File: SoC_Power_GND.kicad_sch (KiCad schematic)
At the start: 4 parts, among them U1 rv1126/rv1109

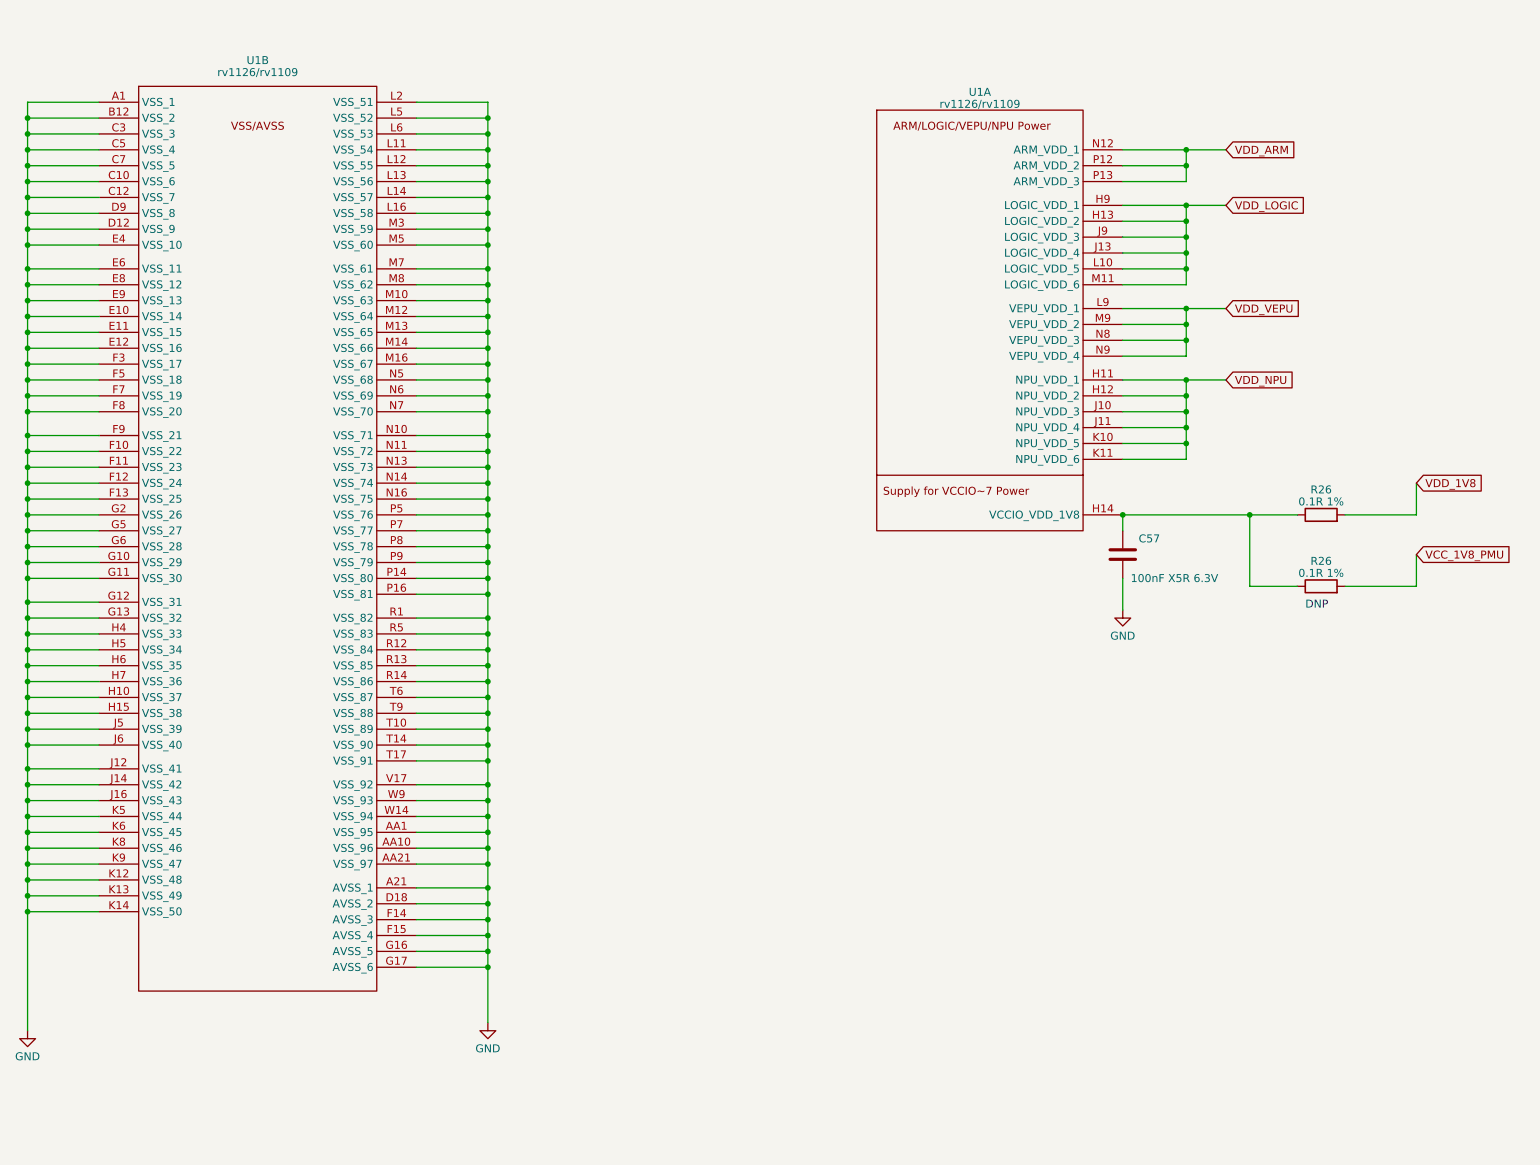
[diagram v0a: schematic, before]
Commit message: updated Power GND
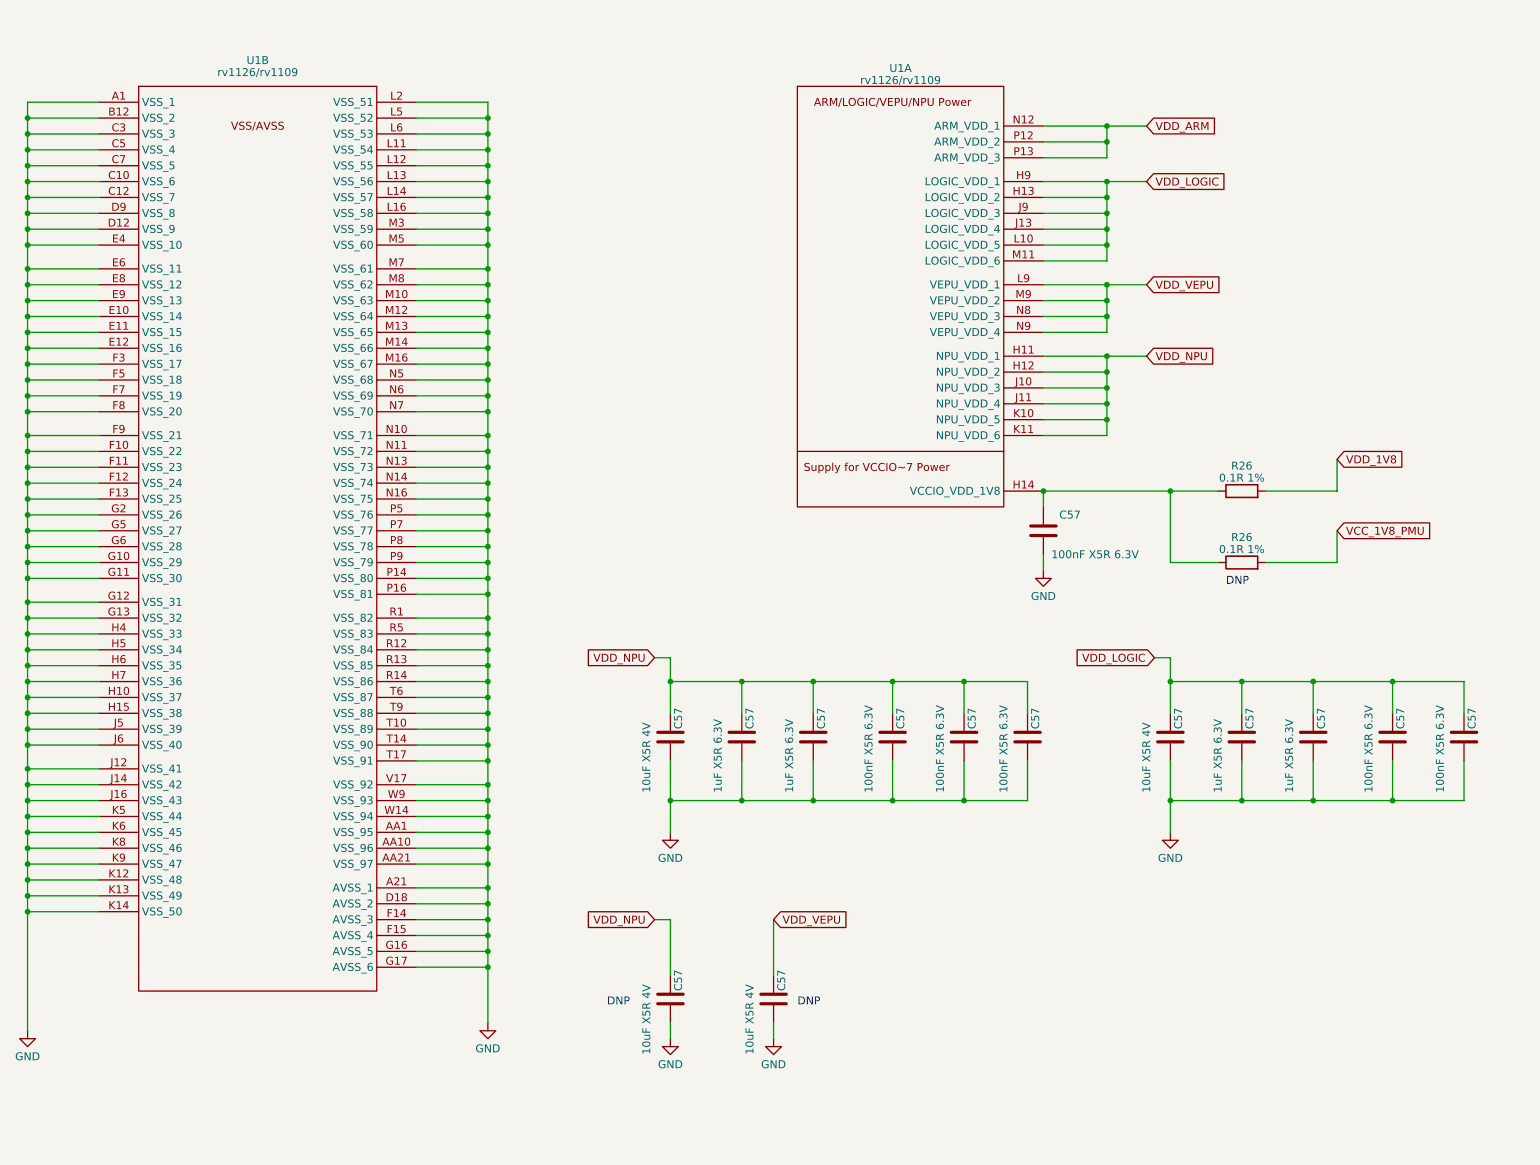
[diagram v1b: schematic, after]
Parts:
- added C57 (x4): 10uF X5R 4V, Capacitor_SMD:C_0402_1005Metric, symbol Device:C
- added C57 (x5): 100nF X5R 6.3V, Capacitor_SMD:C_0201_0603Metric, symbol Device:C
- added C57 (x4): 1uF X5R 6.3V, Capacitor_SMD:C_0402_1005Metric, symbol Device:C
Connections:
- net GND: now also C57.2, C57.2, C57.2, C57.2, C57.2, C57.2, C57.2, C57.2, C57.2, C57.2, C57.2, C57.2, C57.2
- net VDD_LOGIC: now also C57.1, C57.1, C57.1, C57.1, C57.1
- net VDD_NPU: now also C57.1, C57.1, C57.1, C57.1, C57.1, C57.1, C57.1
- net VDD_VEPU: now also C57.1
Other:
- moved on the sheet: C57, R26, U1A

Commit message: added MicroSD
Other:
- note added: "NOTE: If any power domain of VCCIO 1~7 is used, then VCCIO_VDD_1V8 must be connected to 1.8V power supply"
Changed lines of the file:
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@@
     (effects (font (size 1.27 1.27) (color 221 133 0 1)) (justify left bottom))
+  )
+  (text "NOTE:\nIf any power domain of VCCIO 1~7 is used, \nthen VCCIO_VDD_1V8 must be connected to \n1.8V power supply"
+    (at 148.59 104.14 0)
+    (effects (font (size 1.27 1.27) (color 194 194 0 1)) (justify left bottom))
   )
   (text "DNP" (at 234.95 105.41 0)

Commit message: updated footprints
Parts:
- U1: footprint (none) -> Rockchip_SoC:Rockchip_RV1126_FCCSP409LD_14.0x14.0mm
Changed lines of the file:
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@@
         )
         (path "/e3b58043-16a3-43c8-9fad-9c9784eebfa4/cc9fb3ac-19c3-47a8-ba7d-678b4d514ff0/8aa2eca1-edfe-4e9d-a854-96f51e82fbdb"
-          (reference "C95") (unit 1)
+          (reference "C38") (unit 1)
         )
       )
@@
         )
         (path "/e3b58043-16a3-43c8-9fad-9c9784eebfa4/cc9fb3ac-19c3-47a8-ba7d-678b4d514ff0/8aa2eca1-edfe-4e9d-a854-96f51e82fbdb"
-          (reference "C99") (unit 1)
+          (reference "C42") (unit 1)
         )
       )
@@
         )
         (path "/e3b58043-16a3-43c8-9fad-9c9784eebfa4/cc9fb3ac-19c3-47a8-ba7d-678b4d514ff0/8aa2eca1-edfe-4e9d-a854-96f51e82fbdb"
-          (reference "#PWR072") (unit 1)
+          (reference "#PWR060") (unit 1)
         )
       )
@@
       (effects (font (size 1.27 1.27)))
     )
-    (property "Footprint" "" (at 200.66 91.44 0)
+    (property "Footprint" "Rockchip_SoC:Rockchip_RV1126_FCCSP409LD_14.0x14.0mm" (at 200.66 91.44 0)
       (effects (font (size 1.27 1.27)) hide)
     )
@@
         )
         (path "/e3b58043-16a3-43c8-9fad-9c9784eebfa4/cc9fb3ac-19c3-47a8-ba7d-678b4d514ff0/8aa2eca1-edfe-4e9d-a854-96f51e82fbdb"
-          (reference "R33") (unit 1)
+          (reference "R36") (unit 1)
         )
       )
@@
         )
         (path "/e3b58043-16a3-43c8-9fad-9c9784eebfa4/cc9fb3ac-19c3-47a8-ba7d-678b4d514ff0/8aa2eca1-edfe-4e9d-a854-96f51e82fbdb"
-          (reference "C90") (unit 1)
+          (reference "C34") (unit 1)
         )
       )
@@
         )
         (path "/e3b58043-16a3-43c8-9fad-9c9784eebfa4/cc9fb3ac-19c3-47a8-ba7d-678b4d514ff0/8aa2eca1-edfe-4e9d-a854-96f51e82fbdb"
-          (reference "C1") (unit 1)
+          (reference "C29") (unit 1)
         )
       )
@@
         )
         (path "/e3b58043-16a3-43c8-9fad-9c9784eebfa4/cc9fb3ac-19c3-47a8-ba7d-678b4d514ff0/8aa2eca1-edfe-4e9d-a854-96f51e82fbdb"
-          (reference "#PWR071") (unit 1)
+          (reference "#PWR058") (unit 1)
         )
       )
@@
         )
         (path "/e3b58043-16a3-43c8-9fad-9c9784eebfa4/cc9fb3ac-19c3-47a8-ba7d-678b4d514ff0/8aa2eca1-edfe-4e9d-a854-96f51e82fbdb"
-          (reference "#PWR03") (unit 1)
+          (reference "#PWR056") (unit 1)
         )
       )
@@
         )
         (path "/e3b58043-16a3-43c8-9fad-9c9784eebfa4/cc9fb3ac-19c3-47a8-ba7d-678b4d514ff0/8aa2eca1-edfe-4e9d-a854-96f51e82fbdb"
-          (reference "C98") (unit 1)
+          (reference "C41") (unit 1)
         )
       )
@@
         )
         (path "/e3b58043-16a3-43c8-9fad-9c9784eebfa4/cc9fb3ac-19c3-47a8-ba7d-678b4d514ff0/8aa2eca1-edfe-4e9d-a854-96f51e82fbdb"
-          (reference "C94") (unit 1)
+          (reference "C32") (unit 1)
         )
       )
@@
         )
         (path "/e3b58043-16a3-43c8-9fad-9c9784eebfa4/cc9fb3ac-19c3-47a8-ba7d-678b4d514ff0/8aa2eca1-edfe-4e9d-a854-96f51e82fbdb"
-          (reference "C87") (unit 1)
+          (reference "C37") (unit 1)
         )
       )
@@
         )
         (path "/e3b58043-16a3-43c8-9fad-9c9784eebfa4/cc9fb3ac-19c3-47a8-ba7d-678b4d514ff0/8aa2eca1-edfe-4e9d-a854-96f51e82fbdb"
-          (reference "#PWR01") (unit 1)
+          (reference "#PWR054") (unit 1)
         )
       )
@@
         )
         (path "/e3b58043-16a3-43c8-9fad-9c9784eebfa4/cc9fb3ac-19c3-47a8-ba7d-678b4d514ff0/8aa2eca1-edfe-4e9d-a854-96f51e82fbdb"
-          (reference "#PWR069") (unit 1)
+          (reference "#PWR059") (unit 1)
         )
       )
@@
       (effects (font (size 1.27 1.27)))
     )
-    (property "Footprint" "" (at 97.79 90.17 0)
+    (property "Footprint" "Rockchip_SoC:Rockchip_RV1126_FCCSP409LD_14.0x14.0mm" (at 97.79 90.17 0)
       (effects (font (size 1.27 1.27)) hide)
     )
@@
         )
         (path "/e3b58043-16a3-43c8-9fad-9c9784eebfa4/cc9fb3ac-19c3-47a8-ba7d-678b4d514ff0/8aa2eca1-edfe-4e9d-a854-96f51e82fbdb"
-          (reference "#PWR070") (unit 1)
+          (reference "#PWR057") (unit 1)
         )
       )
@@
         )
         (path "/e3b58043-16a3-43c8-9fad-9c9784eebfa4/cc9fb3ac-19c3-47a8-ba7d-678b4d514ff0/8aa2eca1-edfe-4e9d-a854-96f51e82fbdb"
-          (reference "#PWR02") (unit 1)
+          (reference "#PWR055") (unit 1)
         )
       )
@@
         )
         (path "/e3b58043-16a3-43c8-9fad-9c9784eebfa4/cc9fb3ac-19c3-47a8-ba7d-678b4d514ff0/8aa2eca1-edfe-4e9d-a854-96f51e82fbdb"
-          (reference "C93") (unit 1)
+          (reference "C30") (unit 1)
         )
       )
@@
         )
         (path "/e3b58043-16a3-43c8-9fad-9c9784eebfa4/cc9fb3ac-19c3-47a8-ba7d-678b4d514ff0/8aa2eca1-edfe-4e9d-a854-96f51e82fbdb"
-          (reference "C91") (unit 1)
+          (reference "C35") (unit 1)
         )
       )
@@
         )
         (path "/e3b58043-16a3-43c8-9fad-9c9784eebfa4/cc9fb3ac-19c3-47a8-ba7d-678b4d514ff0/8aa2eca1-edfe-4e9d-a854-96f51e82fbdb"
-          (reference "C97") (unit 1)
+          (reference "C40") (unit 1)
         )
       )
@@
         )
         (path "/e3b58043-16a3-43c8-9fad-9c9784eebfa4/cc9fb3ac-19c3-47a8-ba7d-678b4d514ff0/8aa2eca1-edfe-4e9d-a854-96f51e82fbdb"
-          (reference "C88") (unit 1)
+          (reference "C31") (unit 1)
         )
       )
@@
         )
         (path "/e3b58043-16a3-43c8-9fad-9c9784eebfa4/cc9fb3ac-19c3-47a8-ba7d-678b4d514ff0/8aa2eca1-edfe-4e9d-a854-96f51e82fbdb"
-          (reference "C89") (unit 1)
+          (reference "C33") (unit 1)
         )
       )
@@
         )
         (path "/e3b58043-16a3-43c8-9fad-9c9784eebfa4/cc9fb3ac-19c3-47a8-ba7d-678b4d514ff0/8aa2eca1-edfe-4e9d-a854-96f51e82fbdb"
-          (reference "C92") (unit 1)
+          (reference "C36") (unit 1)
         )
       )
@@
         )
         (path "/e3b58043-16a3-43c8-9fad-9c9784eebfa4/cc9fb3ac-19c3-47a8-ba7d-678b4d514ff0/8aa2eca1-edfe-4e9d-a854-96f51e82fbdb"
-          (reference "R34") (unit 1)
+          (reference "R37") (unit 1)
         )
       )
@@
         )
         (path "/e3b58043-16a3-43c8-9fad-9c9784eebfa4/cc9fb3ac-19c3-47a8-ba7d-678b4d514ff0/8aa2eca1-edfe-4e9d-a854-96f51e82fbdb"
-          (reference "C96") (unit 1)
-        )
-      )
+          (reference "C39") (unit 1)
+        )
+      )

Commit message: updated Capacitors
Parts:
- C57: LCSC (none) -> C76934; Model (none) -> GRM033R61A104KE15D; Vendor (none) -> muRata(村田)
- C57: footprint Capacitor_SMD:C_0402_1005Metric -> Capacitor_SMD:C_0201_0603Metric; LCSC (none) -> C76934; Model (none) -> GRM033R61A104KE15D; Vendor (none) -> muRata(村田)
- C57: footprint Capacitor_SMD:C_0402_1005Metric -> Capacitor_SMD:C_0201_0603Metric; LCSC (none) -> C76929; Model (none) -> GRM033R60J105KEA2D; Vendor (none) -> muRata(村田)
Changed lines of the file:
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@@
+      (effects (font (size 1.27 1.27)) hide)
+    )
+    (property "Description" "容值: 100nF 精度: ±10% 额定电压: 10V 材质(温度系数): X5R 材质:X5R" (at 273.05 129.54 0)
+      (effects (font (size 1.27 1.27)) hide)
+    )
+    (property "LCSC" "C76934" (at 273.05 129.54 0)
+      (effects (font (size 1.27 1.27)) hide)
+    )
+    (property "Model" "GRM033R61A104KE15D" (at 273.05 129.54 0)
+      (effects (font (size 1.27 1.27)) hide)
+    )
+    (property "Vendor" "muRata(村田)" (at 273.05 129.54 0)
       (effects (font (size 1.27 1.27)) hide)
     )
@@
       (effects (font (size 1.27 1.27)) hide)
     )
+    (property "Description" "容值: 100nF 精度: ±10% 额定电压: 10V 材质(温度系数): X5R 材质:X5R" (at 181.61 129.54 0)
+      (effects (font (size 1.27 1.27)) hide)
+    )
+    (property "LCSC" "C76934" (at 181.61 129.54 0)
+      (effects (font (size 1.27 1.27)) hide)
+    )
+    (property "Model" "GRM033R61A104KE15D" (at 181.61 129.54 0)
+      (effects (font (size 1.27 1.27)) hide)
+    )
+    (property "Vendor" "muRata(村田)" (at 181.61 129.54 0)
+      (effects (font (size 1.27 1.27)) hide)
+    )
     (pin "1")
     (pin "2")
@@
       (effects (font (size 1.27 1.27)) hide)
     )
+    (property "Description" "容值: 100nF 精度: ±10% 额定电压: 10V 材质(温度系数): X5R 材质:X5R" (at 261.62 129.54 0)
+      (effects (font (size 1.27 1.27)) hide)
+    )
+    (property "LCSC" "C76934" (at 261.62 129.54 0)
+      (effects (font (size 1.27 1.27)) hide)
+    )
+    (property "Model" "GRM033R61A104KE15D" (at 261.62 129.54 0)
+      (effects (font (size 1.27 1.27)) hide)
+    )
+    (property "Vendor" "muRata(村田)" (at 261.62 129.54 0)
+      (effects (font (size 1.27 1.27)) hide)
+    )
     (pin "1")
     (pin "2")
@@
       (effects (font (size 1.27 1.27)) (justify left))
     )
-    (property "Footprint" "Capacitor_SMD:C_0402_1005Metric" (at 206.7052 100.33 0)
+    (property "Footprint" "Capacitor_SMD:C_0201_0603Metric" (at 206.7052 100.33 0)
       (effects (font (size 1.27 1.27)) hide)
     )
     (property "Datasheet" "~" (at 205.74 96.52 0)
+      (effects (font (size 1.27 1.27)) hide)
+    )
+    (property "Description" "容值: 100nF 精度: ±10% 额定电压: 10V 材质(温度系数): X5R 材质:X5R" (at 205.74 96.52 0)
+      (effects (font (size 1.27 1.27)) hide)
+    )
+    (property "LCSC" "C76934" (at 205.74 96.52 0)
+      (effects (font (size 1.27 1.27)) hide)
+    )
+    (property "Model" "GRM033R61A104KE15D" (at 205.74 96.52 0)
+      (effects (font (size 1.27 1.27)) hide)
+    )
+    (property "Vendor" "muRata(村田)" (at 205.74 96.52 0)
       (effects (font (size 1.27 1.27)) hide)
     )
@@
       (effects (font (size 1.27 1.27)) hide)
     )
+    (property "Description" "容值: 100nF 精度: ±10% 额定电压: 10V 材质(温度系数): X5R 材质:X5R" (at 193.04 129.54 0)
+      (effects (font (size 1.27 1.27)) hide)
+    )
+    (property "LCSC" "C76934" (at 193.04 129.54 0)
+      (effects (font (size 1.27 1.27)) hide)
+    )
+    (property "Model" "GRM033R61A104KE15D" (at 193.04 129.54 0)
+      (effects (font (size 1.27 1.27)) hide)
+    )
+    (property "Vendor" "muRata(村田)" (at 193.04 129.54 0)
+      (effects (font (size 1.27 1.27)) hide)
+    )
     (pin "1")
     (pin "2")
@@
       (effects (font (size 1.27 1.27)) (justify left))
     )
-    (property "Footprint" "Capacitor_SMD:C_0402_1005Metric" (at 249.8852 133.35 0)
+    (property "Footprint" "Capacitor_SMD:C_0201_0603Metric" (at 249.8852 133.35 0)
       (effects (font (size 1.27 1.27)) hide)
     )
     (property "Datasheet" "~" (at 248.92 129.54 0)
+      (effects (font (size 1.27 1.27)) hide)
+    )
+    (property "Description" "容值: 1uF 精度: ±10% 额定电压: 6.3V 材质(温度系数): X5R 材质:X5R" (at 248.92 129.54 0)
+      (effects (font (size 1.27 1.27)) hide)
+    )
+    (property "LCSC" "C76929" (at 248.92 129.54 0)
+      (effects (font (size 1.27 1.27)) hide)
+    )
+    (property "Model" "GRM033R60J105KEA2D" (at 248.92 129.54 0)
+      (effects (font (size 1.27 1.27)) hide)
+    )
+    (property "Vendor" "muRata(村田)" (at 248.92 129.54 0)
       (effects (font (size 1.27 1.27)) hide)
     )
@@
       (effects (font (size 1.27 1.27)) (justify left))
     )
-    (property "Footprint" "Capacitor_SMD:C_0402_1005Metric" (at 158.4452 133.35 0)
+    (property "Footprint" "Capacitor_SMD:C_0201_0603Metric" (at 158.4452 133.35 0)
       (effects (font (size 1.27 1.27)) hide)
     )
     (property "Datasheet" "~" (at 157.48 129.54 0)
+      (effects (font (size 1.27 1.27)) hide)
+    )
+    (property "Description" "容值: 1uF 精度: ±10% 额定电压: 6.3V 材质(温度系数): X5R 材质:X5R" (at 157.48 129.54 0)
+      (effects (font (size 1.27 1.27)) hide)
+    )
+    (property "LCSC" "C76929" (at 157.48 129.54 0)
+      (effects (font (size 1.27 1.27)) hide)
+    )
+    (property "Model" "GRM033R60J105KEA2D" (at 157.48 129.54 0)
+      (effects (font (size 1.27 1.27)) hide)
+    )
+    (property "Vendor" "muRata(村田)" (at 157.48 129.54 0)
       (effects (font (size 1.27 1.27)) hide)
     )
@@
       (effects (font (size 1.27 1.27)) (justify left))
     )
-    (property "Footprint" "Capacitor_SMD:C_0402_1005Metric" (at 169.8752 133.35 0)
+    (property "Footprint" "Capacitor_SMD:C_0201_0603Metric" (at 169.8752 133.35 0)
       (effects (font (size 1.27 1.27)) hide)
     )
     (property "Datasheet" "~" (at 168.91 129.54 0)
+      (effects (font (size 1.27 1.27)) hide)
+    )
+    (property "Description" "容值: 1uF 精度: ±10% 额定电压: 6.3V 材质(温度系数): X5R 材质:X5R" (at 168.91 129.54 0)
+      (effects (font (size 1.27 1.27)) hide)
+    )
+    (property "LCSC" "C76929" (at 168.91 129.54 0)
+      (effects (font (size 1.27 1.27)) hide)
+    )
+    (property "Model" "GRM033R60J105KEA2D" (at 168.91 129.54 0)
+      (effects (font (size 1.27 1.27)) hide)
+    )
+    (property "Vendor" "muRata(村田)" (at 168.91 129.54 0)
       (effects (font (size 1.27 1.27)) hide)
     )
@@
     )
     (property "Datasheet" "~" (at 203.2 129.54 0)
+      (effects (font (size 1.27 1.27)) hide)
+    )
+    (property "Description" "容值: 100nF 精度: ±10% 额定电压: 10V 材质(温度系数): X5R 材质:X5R" (at 203.2 129.54 0)
+      (effects (font (size 1.27 1.27)) hide)
+    )
+    (property "LCSC" "C76934" (at 203.2 129.54 0)
+      (effects (font (size 1.27 1.27)) hide)
+    )
+    (property "Model" "GRM033R61A104KE15D" (at 203.2 129.54 0)
+      (effects (font (size 1.27 1.27)) hide)
+    )
+    (property "Vendor" "muRata(村田)" (at 203.2 129.54 0)
       (effects (font (size 1.27 1.27)) hide)
     )
@@
       (effects (font (size 1.27 1.27)) (justify left))
     )
-    (property "Footprint" "Capacitor_SMD:C_0402_1005Metric" (at 238.4552 133.35 0)
+    (property "Footprint" "Capacitor_SMD:C_0201_0603Metric" (at 238.4552 133.35 0)
       (effects (font (size 1.27 1.27)) hide)
     )
@@
       (effects (font (size 1.27 1.27)) hide)
     )
+    (property "Description" "容值: 1uF 精度: ±10% 额定电压: 6.3V 材质(温度系数): X5R 材质:X5R" (at 237.49 129.54 0)
+      (effects (font (size 1.27 1.27)) hide)
+    )
+    (property "LCSC" "C76929" (at 237.49 129.54 0)
+      (effects (font (size 1.27 1.27)) hide)
+    )
+    (property "Model" "GRM033R60J105KEA2D" (at 237.49 129.54 0)
+      (effects (font (size 1.27 1.27)) hide)
+    )
+    (property "Vendor" "muRata(村田)" (at 237.49 129.54 0)
+      (effects (font (size 1.27 1.27)) hide)
+    )
